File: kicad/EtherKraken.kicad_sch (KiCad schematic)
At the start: 56 parts, among them IC1 NCV33375ST3.3T3G, IC2 NCV33375ST3.3T3G, J1 Conn_02x03_Odd_Even, J2 Conn_02x10_Odd_Even, J3 RJ45_Wuerth_7499010121A, J4 Conn_02x10_Odd_Even, J5 Conn_02x10_Odd_Even, U1 RASPBERRY_PI_ZERO_2_W, U2 AT45DB641E-SHN-T, U3 W5500, U4 MCP23017x-x-SO, U5 MCP23017x-x-SO, Y1 25MHz

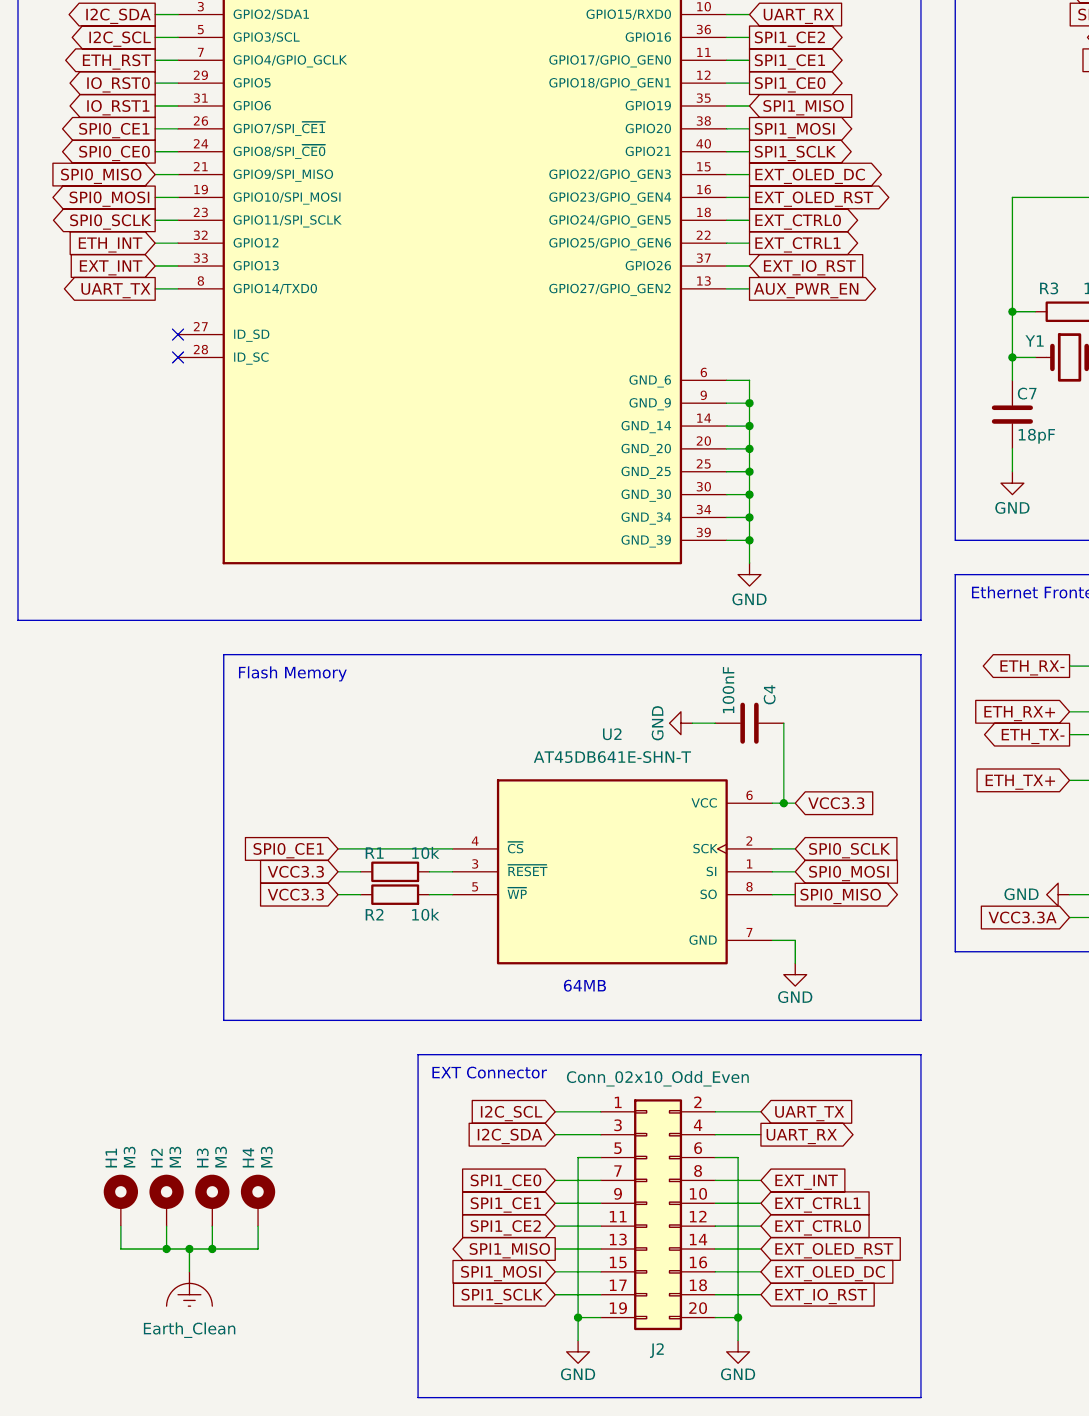
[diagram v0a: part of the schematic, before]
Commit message: Implement basic board initialization and flash interface in HAL
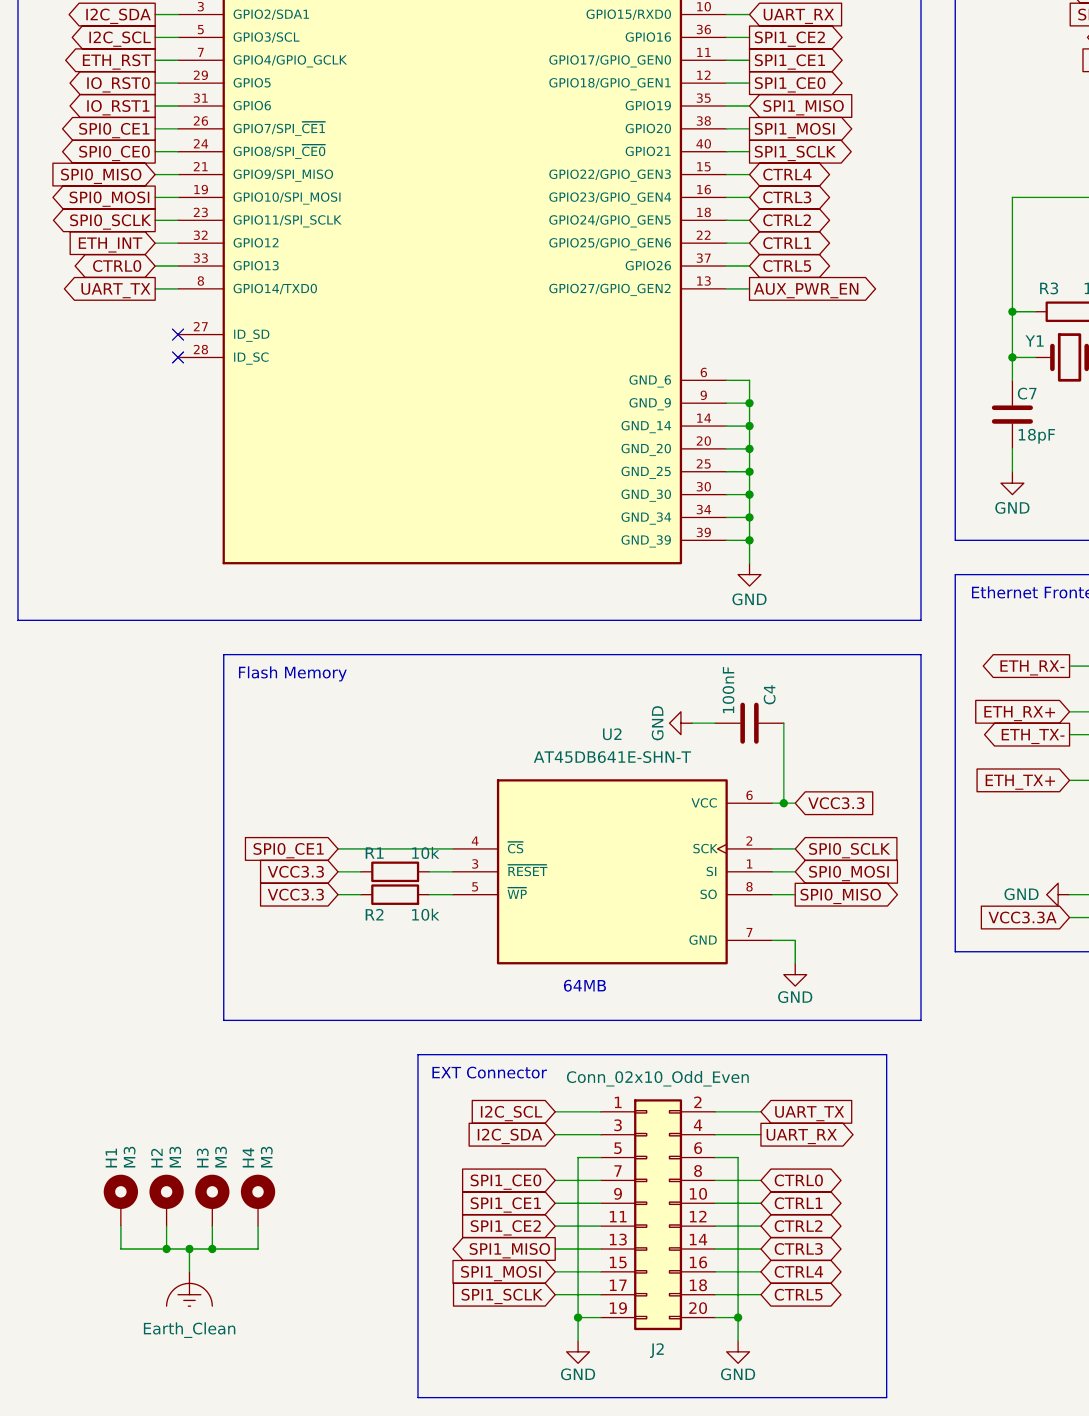
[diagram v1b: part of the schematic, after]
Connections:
- net EXT_CTRL0 renamed CTRL2
- net EXT_CTRL1 renamed CTRL1
- net EXT_INT renamed CTRL0
- net EXT_IO_RST renamed CTRL5
- net EXT_OLED_DC renamed CTRL4
- net EXT_OLED_RST renamed CTRL3
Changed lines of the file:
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@@
 	(rectangle
 		(start 69.85 213.36)
-		(end 125.73 251.46)
+		(end 121.92 251.46)
 		(stroke
 			(width 0)
@@
 		)
 	)
-	(global_label "EXT_CTRL1"
-		(shape output)
+	(global_label "CTRL1"
+		(shape bidirectional)
 		(at 106.68 123.19 0)
 		(fields_autoplaced yes)
@@
 		)
 		(property "Intersheetrefs" "${INTERSHEET_REFS}"
-			(at 119.7041 123.19 0)
+			(at 116.5217 123.19 0)
 			(hide yes)
 			(show_name no)
@@
 		)
 	)
-	(global_label "EXT_INT"
-		(shape input)
+	(global_label "CTRL0"
+		(shape bidirectional)
 		(at 107.95 227.33 0)
 		(fields_autoplaced yes)
@@
 		)
 		(property "Intersheetrefs" "${INTERSHEET_REFS}"
-			(at 118.1318 227.33 0)
+			(at 117.7917 227.33 0)
 			(hide yes)
 			(show_name no)
@@
 		)
 	)
-	(global_label "EXT_CTRL1"
-		(shape input)
+	(global_label "CTRL1"
+		(shape bidirectional)
 		(at 107.95 229.87 0)
 		(fields_autoplaced yes)
@@
 		)
 		(property "Intersheetrefs" "${INTERSHEET_REFS}"
-			(at 120.9741 229.87 0)
+			(at 117.7917 229.87 0)
 			(hide yes)
 			(show_name no)
@@
 		)
 	)
-	(global_label "EXT_IO_RST"
-		(shape input)
+	(global_label "CTRL5"
+		(shape bidirectional)
 		(at 107.95 240.03 0)
 		(fields_autoplaced yes)
@@
 		)
 		(property "Intersheetrefs" "${INTERSHEET_REFS}"
-			(at 121.5789 240.03 0)
+			(at 117.7917 240.03 0)
 			(hide yes)
 			(show_name no)
@@
 		)
 	)
-	(global_label "EXT_CTRL0"
-		(shape input)
+	(global_label "CTRL2"
+		(shape bidirectional)
 		(at 107.95 232.41 0)
 		(fields_autoplaced yes)
@@
 		)
 		(property "Intersheetrefs" "${INTERSHEET_REFS}"
-			(at 120.9741 232.41 0)
+			(at 117.7917 232.41 0)
 			(hide yes)
 			(show_name no)
@@
 		)
 	)
-	(global_label "EXT_OLED_DC"
-		(shape output)
+	(global_label "CTRL4"
+		(shape bidirectional)
 		(at 106.68 115.57 0)
 		(fields_autoplaced yes)
@@
 		)
 		(property "Intersheetrefs" "${INTERSHEET_REFS}"
-			(at 122.2441 115.57 0)
+			(at 116.5217 115.57 0)
 			(hide yes)
 			(show_name no)
@@
 		)
 	)
-	(global_label "EXT_OLED_RST"
-		(shape input)
+	(global_label "CTRL3"
+		(shape bidirectional)
 		(at 107.95 234.95 0)
 		(fields_autoplaced yes)
@@
 		)
 		(property "Intersheetrefs" "${INTERSHEET_REFS}"
-			(at 124.4212 234.95 0)
+			(at 117.7917 234.95 0)
 			(hide yes)
 			(show_name no)
@@
 		)
 	)
-	(global_label "EXT_CTRL0"
-		(shape output)
+	(global_label "CTRL2"
+		(shape bidirectional)
 		(at 106.68 120.65 0)
 		(fields_autoplaced yes)
@@
 		)
 		(property "Intersheetrefs" "${INTERSHEET_REFS}"
-			(at 119.7041 120.65 0)
+			(at 116.5217 120.65 0)
 			(hide yes)
 			(show_name no)
@@
 		)
 	)
-	(global_label "EXT_OLED_RST"
-		(shape output)
+	(global_label "CTRL3"
+		(shape bidirectional)
 		(at 106.68 118.11 0)
 		(fields_autoplaced yes)
@@
 		)
 		(property "Intersheetrefs" "${INTERSHEET_REFS}"
-			(at 123.1512 118.11 0)
+			(at 116.5217 118.11 0)
 			(hide yes)
 			(show_name no)
@@
 		)
 	)
-	(global_label "EXT_INT"
-		(shape input)
+	(global_label "CTRL0"
+		(shape bidirectional)
 		(at 40.64 125.73 180)
 		(fields_autoplaced yes)
@@
 		)
 		(property "Intersheetrefs" "${INTERSHEET_REFS}"
-			(at 30.4582 125.73 0)
+			(at 30.7983 125.73 0)
 			(hide yes)
 			(show_name no)
@@
 		)
 	)
-	(global_label "EXT_IO_RST"
-		(shape input)
+	(global_label "CTRL5"
+		(shape bidirectional)
 		(at 106.68 125.73 0)
 		(fields_autoplaced yes)
@@
 		)
 		(property "Intersheetrefs" "${INTERSHEET_REFS}"
-			(at 120.3089 125.73 0)
+			(at 116.5217 125.73 0)
 			(hide yes)
 			(show_name no)
@@
 		)
 	)
-	(global_label "EXT_OLED_DC"
-		(shape input)
+	(global_label "CTRL4"
+		(shape bidirectional)
 		(at 107.95 237.49 0)
 		(fields_autoplaced yes)
@@
 		)
 		(property "Intersheetrefs" "${INTERSHEET_REFS}"
-			(at 123.5141 237.49 0)
+			(at 117.7917 237.49 0)
 			(hide yes)
 			(show_name no)

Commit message: Update KiCad files for Revision B
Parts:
- removed J4: Conn_02x10_Odd_Even, parts:09185206324_02x10_P2.54, symbol Connector_Generic:Conn_02x10_Odd_Even
- removed R2: 10k, Resistor_SMD:R_1206_3216Metric, symbol Device:R
- removed U5: MCP23017x-x-SO, Package_SO:SOIC-28W_7.5x17.9mm_P1.27mm, symbol Interface_Expansion:MCP23017x-x-SO
- added C22: 18pF, Capacitor_SMD:C_1206_3216Metric, symbol Device:C
- added C23, C24, C25, C26, C27, C30: 100nF, Capacitor_SMD:C_1206_3216Metric, symbol Device:C
- added C28: 22pF, Capacitor_SMD:C_1206_3216Metric, symbol Device:C
- added C29: 33pF, Capacitor_SMD:C_1206_3216Metric, symbol Device:C
- added D4, D5, D6, D7: LED, LED_SMD:LED_1206_3216Metric, symbol Device:LED
- added J3: Conn_02x10_Odd_Even, parts:09185206324_02x10_P2.54, symbol Connector_Generic:Conn_02x10_Odd_Even
- added Q1, Q2, Q3, Q4: MMBT3904, Package_TO_SOT_SMD:SOT-23, symbol Transistor_BJT:MMBT3904
- added R14, R16, R18, R20: 1,2k, Resistor_SMD:R_1206_3216Metric, symbol Device:R
- added R15, R17, R19, R21: 62R, Resistor_SMD:R_1206_3216Metric, symbol Device:R
- added R22: 10k, Resistor_SMD:R_1206_3216Metric, symbol Device:R
- added U5: STM32F071CBTx, Package_QFP:LQFP-48_7x7mm_P0.5mm, symbol MCU_ST_STM32F0:STM32F071CBTx
- added U6: SC16IS740, Package_SO:TSSOP-16_4.4x5mm_P0.65mm, symbol Interface_UART:SC16IS740
- added Y2: 8MHz, Crystal:Crystal_HC49-U_Vertical, symbol Device:Crystal
- added Y3: 1,8432MHz, Crystal:Crystal_HC49-U_Vertical, symbol Device:Crystal
- C17: value 100nF -> 10nF
- C21: value 100nF -> 18pF
- D1, D2, D3: footprint LED_THT:LED_D3.0mm -> LED_SMD:LED_1206_3216Metric
- RN1: value 3,3R -> 33R; footprint Resistor_SMD:R_Array_Convex_4x1206 -> parts:R_Array_Convex_8N_1206
- renumbered C11 to C10, C10 to C11, J3 to J4, R11 to R10, R12 to R11, R13 to R12, R14 to R13, R3 to R2, R4 to R3, R5 to R4, R6 to R5, R7 to R6, R8 to R7, R9 to R8, R10 to R9
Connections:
- net IO_RST1 is gone; now on net IO_RST: U1.31 (GPIO6)
- net AUX_PWR_EN: now also J2.18 (Pin_18)
- net ETH_RST: now also U1.33 (GPIO13); no longer U1.7 (GPIO4/GPIO_GCLK)
- net GND: now also C21.2, J2.7 (Pin_7), C22.2, C23.2, C24.2, C25.1, C26.1, C27.1, C28.2, C29.2, C30.2, J3.1 (Pin_1), J3.19 (Pin_19), J3.2 (Pin_2), J3.20 (Pin_20), Q1.2 (E), Q2.2 (E), Q3.2 (E), Q4.2 (E), U5.23 (VSS), U5.35 (VSS), U5.47 (VSS), U5.8 (VSSA), U6.2 (A0/~{CS}), U6.3 (A1/SI), U6.9 (VSS); no longer C21.1
- net I2C_SCL: now also U6.5 (SCL/SCLK)
- net I2C_SDA: now also U6.6 (SDA)
- net SPI1_CE0: now also U5.25 (PB12); no longer J2.7 (Pin_7)
- net SPI1_MISO: now also U5.27 (PB14)
- net SPI1_MOSI: now also U5.28 (PB15)
- net SPI1_SCLK: now also U5.26 (PB13)
- net VCC3.3: now also U2.5 (~{WP}), C23.1, C24.1, C25.2, C26.2, C27.2, C30.1, R22.2, U5.1 (VBAT), U5.24 (VDD), U5.36 (VDDIO2), U5.48 (VDD), U5.9 (VDDA), U6.1 (VDD), U6.8 (I2C/~{SPI}); no longer C21.2
- net VCC5: now also D4.2 (A), D5.2 (A), D6.2 (A), D7.2 (A)
- net IO_B6: now reaches J5.4 (Pin_4)
- net IO_B6: now also U4.27 (GPA6)
- net IO_B7: now reaches J5.6 (Pin_6)
- net IO_B7: now also U4.28 (GPA7)
- net IO_A10: now reaches J5.3 (Pin_3)
- net IO_A10: now also U5.19 (PB1)
- net IO_A11: now reaches J5.5 (Pin_5)
- net IO_A11: now also U5.20 (PB2)
- net IO_A12: now reaches J5.7 (Pin_7)
- net IO_A12: now also U5.39 (PB3)
- net IO_A13: now reaches J5.9 (Pin_9)
- net IO_A13: now also U5.34 (PA13)
- net IO_A14: now reaches J5.11 (Pin_11)
- net IO_A14: now also U5.37 (PA14)
- net IO_A15: now reaches J5.13 (Pin_13)
- net IO_A15: now also U5.38 (PA15)
- net IO_A16: now reaches J5.15 (Pin_15)
- net IO_A16: now also U5.40 (PB4)
- net IO_A17: now reaches J5.17 (Pin_17)
- net IO_A17: now also U5.41 (PB5)
- net IO_B8: now reaches J5.8 (Pin_8)
- net IO_B8: now also U4.1 (GPB0)
- net IO_B9: now reaches J5.10 (Pin_10)
- net IO_B9: now also U4.2 (GPB1)
- net IO_B10: now reaches J5.12 (Pin_12)
- net IO_B10: now also U4.3 (GPB2)
- net IO_B11: now reaches J5.14 (Pin_14)
- net IO_B11: now also U4.4 (GPB3)
- net IO_A18: now reaches J5.16 (Pin_16)
- net IO_A18: now also U5.42 (PB6)
- net IO_A19: now reaches J5.18 (Pin_18)
- net IO_A19: now also U5.43 (PB7)
- net IO_B4: now reaches U4.25 (GPA4)
- net IO_B4: now also J3.12 (Pin_12)
- net ST_LED0: now reaches U4.5 (GPB4)
- net ST_LED0: now also R14.1
- net IO_B5: now reaches U4.26 (GPA5)
- net IO_B5: now also J3.14 (Pin_14)
- net ST_LED1: now reaches U4.6 (GPB5)
- net ST_LED1: now also R16.1
- net ST_LED2: now reaches U4.7 (GPB6)
- net ST_LED2: now also R18.1
- net ST_LED3: now reaches U4.8 (GPB7)
- net ST_LED3: now also R20.1
- net IO_B0: now reaches U4.21 (GPA0)
- net IO_B0: now also J3.4 (Pin_4)
- net IO_B1: now reaches U4.22 (GPA1)
- net IO_B1: now also J3.6 (Pin_6)
- net IO_B2: now reaches U4.23 (GPA2)
- net IO_B2: now also J3.8 (Pin_8)
- net IO_B3: now reaches U4.24 (GPA3)
- net IO_B3: now also J3.10 (Pin_10)
- net IO_INT1: now reaches U4.19 (INTB)
- net IO_INT1: now also U1.29 (GPIO5)
- net IO_INT0: now reaches U4.20 (INTA)
- net IO_INT0: now also U1.7 (GPIO4/GPIO_GCLK)
- net CTRL0 renamed CO_RST
- net CO_RST: now also U1.15 (GPIO22/GPIO_GEN3), U5.7 (NRST); no longer U1.33 (GPIO13)
- net CTRL1 renamed AUX0
- net AUX0: now also J2.14 (Pin_14); no longer J2.10 (Pin_10)
- net CTRL2 renamed CO_SINT
- net CO_SINT: now also U6.7 (~{IRQ})
- net CTRL3 renamed CO_BOOT
- net CO_BOOT: now also J2.10 (Pin_10), U5.44 (BOOT0); no longer J2.14 (Pin_14)
- net CTRL4 renamed AUX1
- net AUX1: now also U1.37 (GPIO26); no longer U1.15 (GPIO22/GPIO_GEN3)
- removed net CTRL5: J2.18 (Pin_18), U1.37 (GPIO26)
- net IO_RST0 renamed IO_RST
- net IO_RST: no longer U1.29 (GPIO5)
- new net: C21.1, U5.5 (PF0), Y2.1
- new net: C22.1, U5.6 (PF1), Y2.2
- new net: C29.1, U6.16 (XTAL2), Y3.2
- new net: Q1.3 (C), R15.1
- new net: D4.1 (K), R15.2
- new net: D7.1 (K), R21.2
- new net: Q1.1 (B), R14.2
- new net: C28.1, U6.15 (XTAL1), Y3.1
- new net: Q3.1 (B), R18.2
- new net: Q3.3 (C), R19.1
- new net: Q4.3 (C), R21.1
- new net: Q2.1 (B), R16.2
- new net: Q4.1 (B), R20.2
- new net: D6.1 (K), R19.2
- new net: Q2.3 (C), R17.1
- new net: D5.1 (K), R17.2
- new net: R22.1, U6.14 (~{RESET})
- new net CO_SCTS: U5.32 (PA11), U6.10 (~{RTS})
- new net CO_SRTS: U5.33 (PA12), U6.11 (~{CTS})
- new net CO_SRX: U5.31 (PA10), U6.12 (TX)
- new net CO_STX: U5.30 (PA9), U6.13 (RX)
- new net IO_A0: J3.3 (Pin_3), U5.10 (PA0)
- new net IO_A1: J3.5 (Pin_5), U5.11 (PA1)
- new net IO_A2: J3.7 (Pin_7), U5.12 (PA2)
- new net IO_A3: J3.9 (Pin_9), U5.13 (PA3)
- new net IO_A4: J3.11 (Pin_11), U5.14 (PA4)
- new net IO_A5: J3.13 (Pin_13), U5.15 (PA5)
- new net IO_A6: J3.15 (Pin_15), U5.16 (PA6)
- new net IO_A7: J3.17 (Pin_17), U5.17 (PA7)
- new net IO_A8: J3.16 (Pin_16), U5.29 (PA8)
- new net IO_A9: J3.18 (Pin_18), U5.18 (PB0)
- no-connect marks 20 -> 24
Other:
- note added: "Coprocessor"
- note added: "Coprocessor UART"
- note added: "IO MUX"
- note added: "IO0 Connector"
- note added: "IO1 Connector"
- note added: "I²C Address 0x48"
- note added: "Status LEDs"
- note added: "to SPI2"
- note removed: "IO MUX 0"
- note removed: "IO MUX 1"
- note removed: "I²C Address 0x21"
- moved on the sheet: C1, C10, C11, C12, C13, C14, C15, C16, C17, C18, C19, C2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

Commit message: Split single A2 sheet for schematic into multiple A4 sub schematics
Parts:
- removed C1: 2,2µF, Capacitor_THT:CP_Radial_D5.0mm_P2.00mm, symbol Device:C_Polarized
- removed C10, C12, C14, C2, C20, C23, C24, C25, C26, C27, C30, C4, C6: 100nF, Capacitor_SMD:C_1206_3216Metric, symbol Device:C
- removed C11, C3: 4,7µF, Capacitor_THT:CP_Radial_D5.0mm_P2.00mm, symbol Device:C_Polarized
- removed C13, C5: 10µF, Capacitor_THT:CP_Radial_D5.0mm_P2.00mm, symbol Device:C_Polarized
- removed C15, C16: 6.8nF, Capacitor_SMD:C_1206_3216Metric, symbol Device:C
- removed C17, C18: 10nF, Capacitor_SMD:C_1206_3216Metric, symbol Device:C
- removed C19: 4.7µF, Capacitor_THT:CP_Radial_D5.0mm_P2.00mm, symbol Device:C_Polarized
- removed C21, C22, C7, C8: 18pF, Capacitor_SMD:C_1206_3216Metric, symbol Device:C
- removed C28: 22pF, Capacitor_SMD:C_1206_3216Metric, symbol Device:C
- removed C29: 33pF, Capacitor_SMD:C_1206_3216Metric, symbol Device:C
- removed C9: 22nF, Capacitor_SMD:C_1206_3216Metric, symbol Device:C
- removed D1, D2, D3, D4, D5, D6, D7: LED, LED_SMD:LED_1206_3216Metric, symbol Device:LED
- removed IC1, IC2: NCV33375ST3.3T3G, parts:SOT230P700X175-4N, symbol parts:NCV33375ST3.3T3G
- removed J1: Conn_02x03_Odd_Even, parts:09185066324_02x03_P2.54, symbol Connector_Generic:Conn_02x03_Odd_Even
- removed J2, J3, J5: Conn_02x10_Odd_Even, parts:09185206324_02x10_P2.54, symbol Connector_Generic:Conn_02x10_Odd_Even
- removed J4: RJ45_Wuerth_7499010121A, Connector_RJ:RJ45_Wuerth_7499010121A_Horizontal, symbol Connector:RJ45_Wuerth_7499010121A
- removed Q1, Q2, Q3, Q4: MMBT3904, Package_TO_SOT_SMD:SOT-23, symbol Transistor_BJT:MMBT3904
- removed R1, R22: 10k, Resistor_SMD:R_1206_3216Metric, symbol Device:R
- removed R10: 12.4k, Resistor_SMD:R_1206_3216Metric, symbol Device:R
- removed R11, R12: 51R, Resistor_SMD:R_1206_3216Metric, symbol Device:R
- removed R13: 150R, Resistor_SMD:R_1206_3216Metric, symbol Device:R
- removed R14, R16, R18, R20: 1,2k, Resistor_SMD:R_1206_3216Metric, symbol Device:R
- removed R15, R17, R19, R21: 62R, Resistor_SMD:R_1206_3216Metric, symbol Device:R
- removed R2: 1M, Resistor_SMD:R_1206_3216Metric, symbol Device:R
- removed R3, R4, R6, R7: 49,9R, Resistor_SMD:R_1206_3216Metric, symbol Device:R
- removed R5: 10R, Resistor_SMD:R_1206_3216Metric, symbol Device:R
- removed R8, R9: 330R, Resistor_SMD:R_1206_3216Metric, symbol Device:R
- removed RN1: 33R, parts:R_Array_Convex_8N_1206, symbol Device:R_Pack04
- removed U1: RASPBERRY_PI_ZERO_2_W, parts:MODULE_RASPBERRY_PI_ZERO_2_W, symbol parts:RASPBERRY_PI_ZERO_2_W
- removed U2: AT45DB641E-SHN-T, Package_SO:SOIC-8_5.3x5.3mm_P1.27mm, symbol parts:AT45DB641E-SHN-T
- removed U3: W5500, Package_QFP:LQFP-48_7x7mm_P0.5mm, symbol Interface_Ethernet:W5500
- removed U4: MCP23017x-x-SO, Package_SO:SOIC-28W_7.5x17.9mm_P1.27mm, symbol Interface_Expansion:MCP23017x-x-SO
- removed U5: STM32F071CBTx, Package_QFP:LQFP-48_7x7mm_P0.5mm, symbol MCU_ST_STM32F0:STM32F071CBTx
- removed U6: SC16IS740, Package_SO:TSSOP-16_4.4x5mm_P0.65mm, symbol Interface_UART:SC16IS740
- removed Y1: 25MHz, Crystal:Crystal_HC49-U_Vertical, symbol Device:Crystal
- removed Y2: 8MHz, Crystal:Crystal_HC49-U_Vertical, symbol Device:Crystal
- removed Y3: 1,8432MHz, Crystal:Crystal_HC49-U_Vertical, symbol Device:Crystal
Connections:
- no-connect marks 24 -> 0
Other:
- added sheet Coprocessor (Coprocessor.kicad_sch)
- added sheet Ethernet PHY (Ethernet PHY.kicad_sch)
- added sheet Fan Controller (Fan Controller.kicad_sch)
- added sheet IO (IO.kicad_sch)
- added sheet Main Processor (Main Processor.kicad_sch)
- added sheet Power Conditioning (Power Conditioning.kicad_sch)
- note removed: "64MB"
- note removed: "ARM64 MCU"
- note removed: "AUX PWR Regulation"
- note removed: "Coprocessor"
- note removed: "Coprocessor UART"
- note removed: "EXT Connector"
- note removed: "Ethernet Frontend"
- note removed: "Ethernet Frontend PWR Regulation"
- note removed: "Ethernet PHY"
- note removed: "Flash Memory"
- note removed: "IO MUX"
- note removed: "IO0 Connector"
- note removed: "IO1 Connector"
- note removed: "I²C Address 0x20"
- note removed: "I²C Address 0x48"
- note removed: "PWR LEDs"
- note removed: "Power In 5V @ 600mA"
- note removed: "Status LEDs"
- note removed: "to SPI2"
- moved on the sheet: H1, H2, H3, H4
